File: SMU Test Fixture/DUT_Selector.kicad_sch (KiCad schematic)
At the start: 19 parts

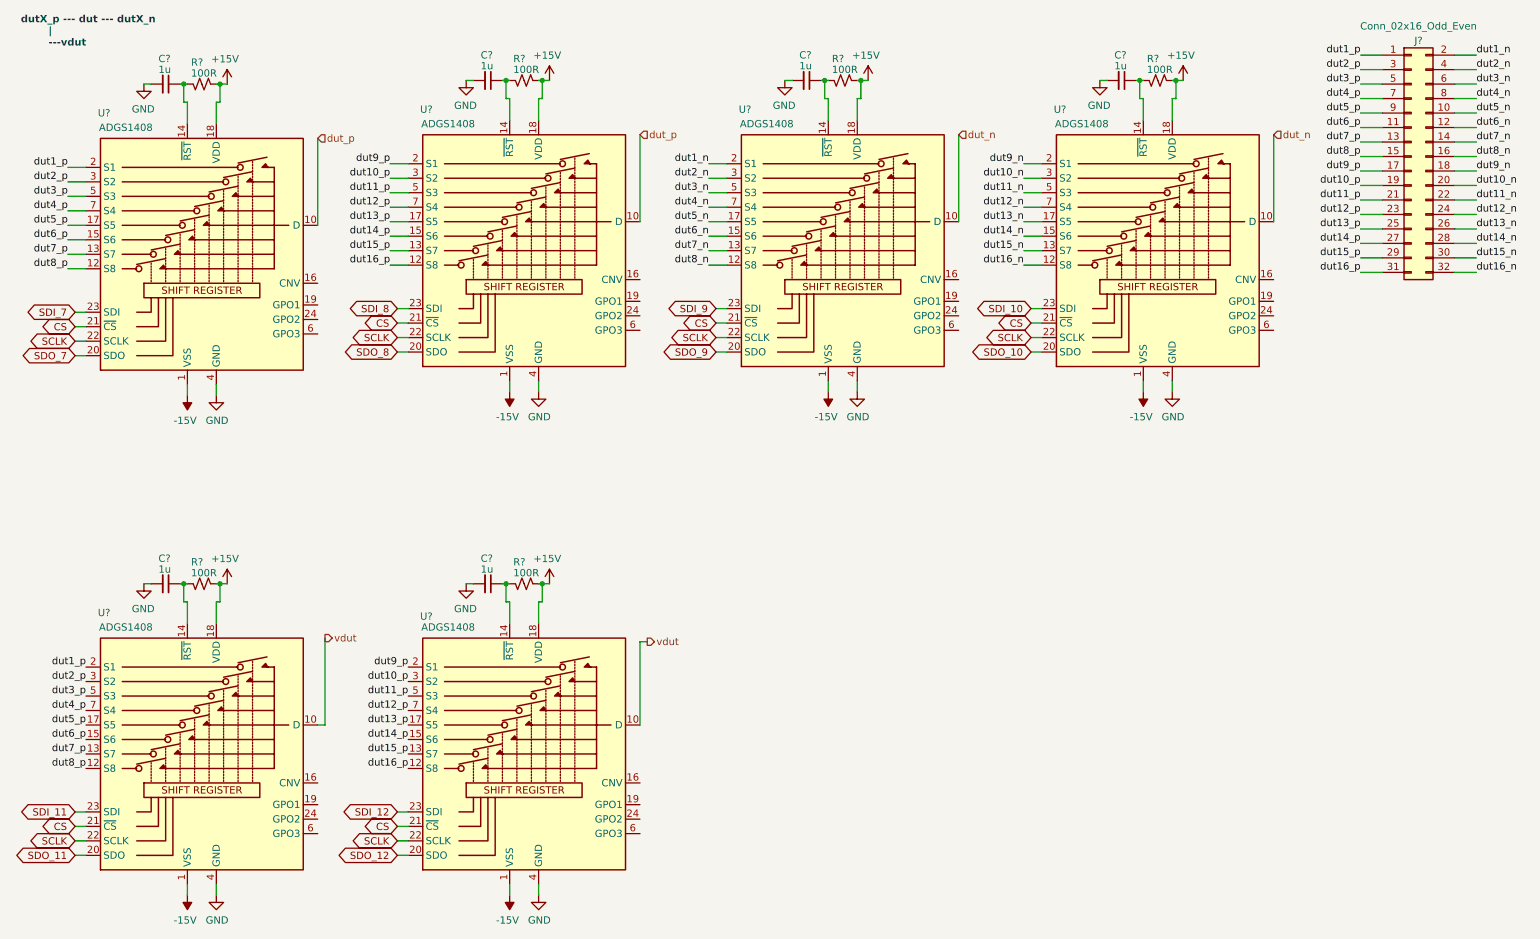
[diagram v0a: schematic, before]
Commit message: Fix grid nightmare. Begin adding bypass caps for a.switches
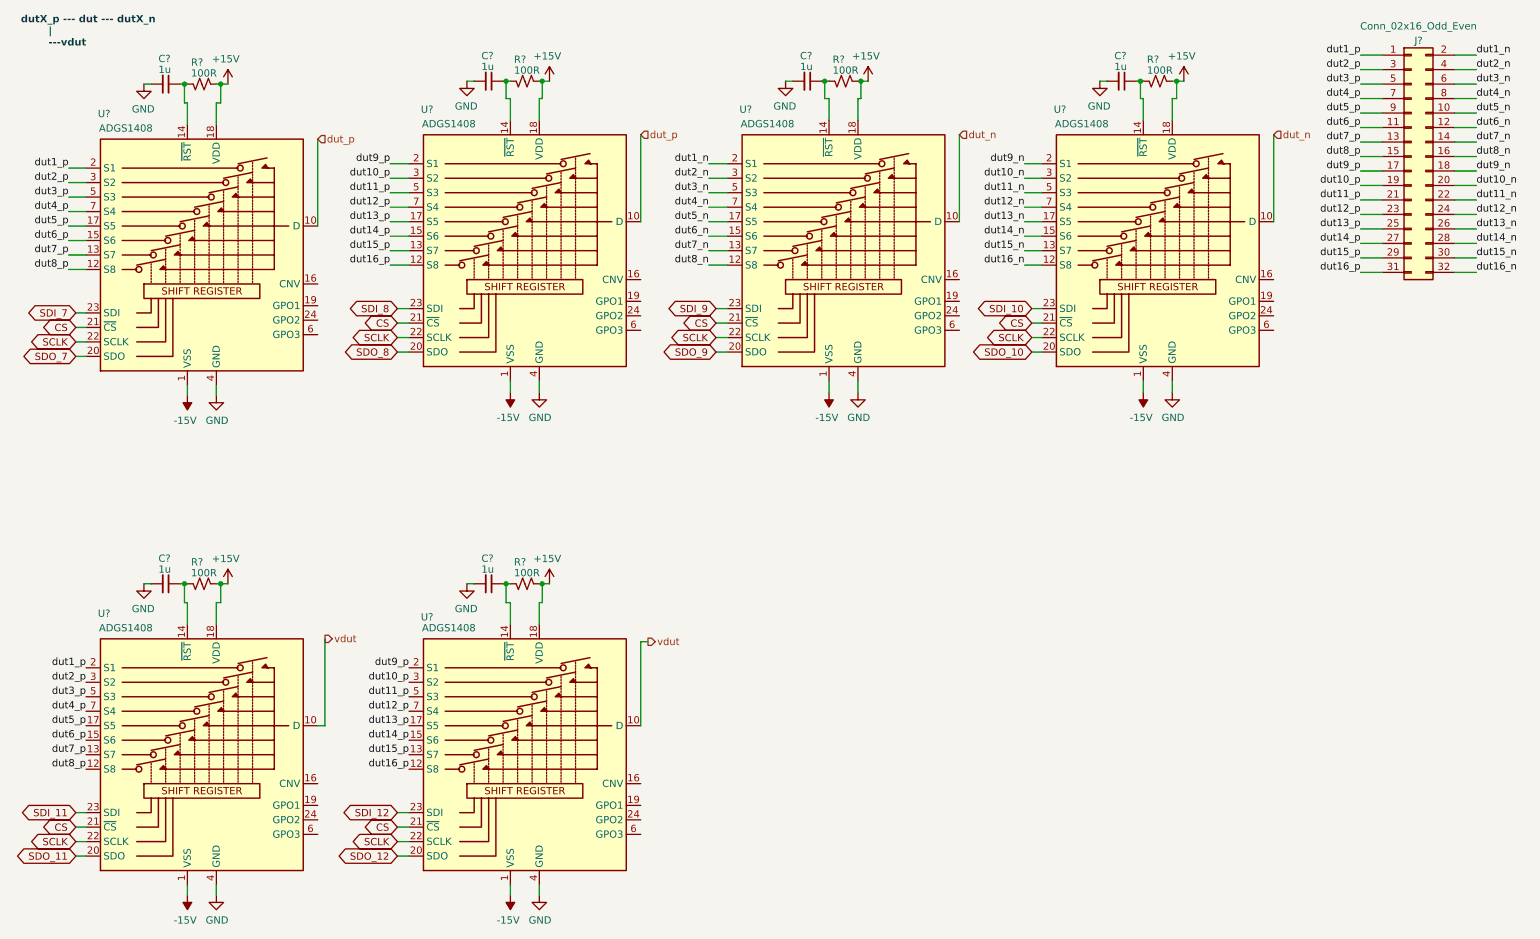
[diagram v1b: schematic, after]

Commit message: Finish adding bypass for all a.switches
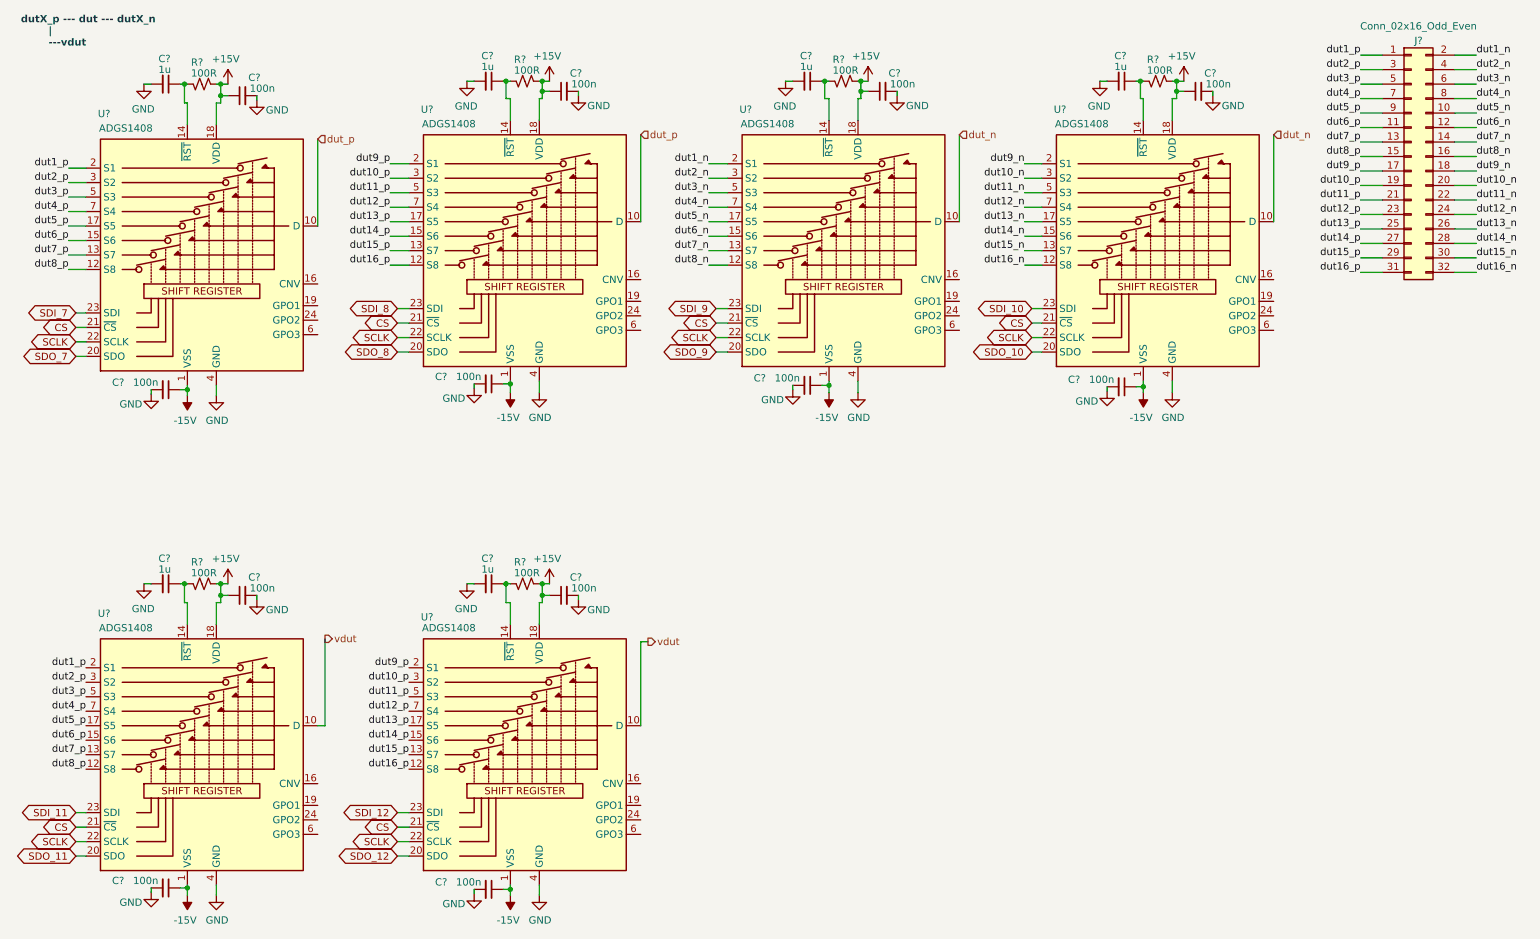
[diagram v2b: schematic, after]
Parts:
- added C? (x12): 100n, Capacitor_SMD:C_0805_2012Metric_Pad1.18x1.45mm_HandSolder, symbol Device:C_Small
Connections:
- net +15V: now also C?.1, C?.1, C?.1, C?.1, C?.1, C?.1
- net -15V: now also C?.1, C?.1, C?.1, C?.1, C?.1, C?.1
- net GND: now also C?.2, C?.2, C?.2, C?.2, C?.2, C?.2, C?.2, C?.2, C?.2, C?.2, C?.2, C?.2

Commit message: Split ADGS1408 units, add switch contorl page
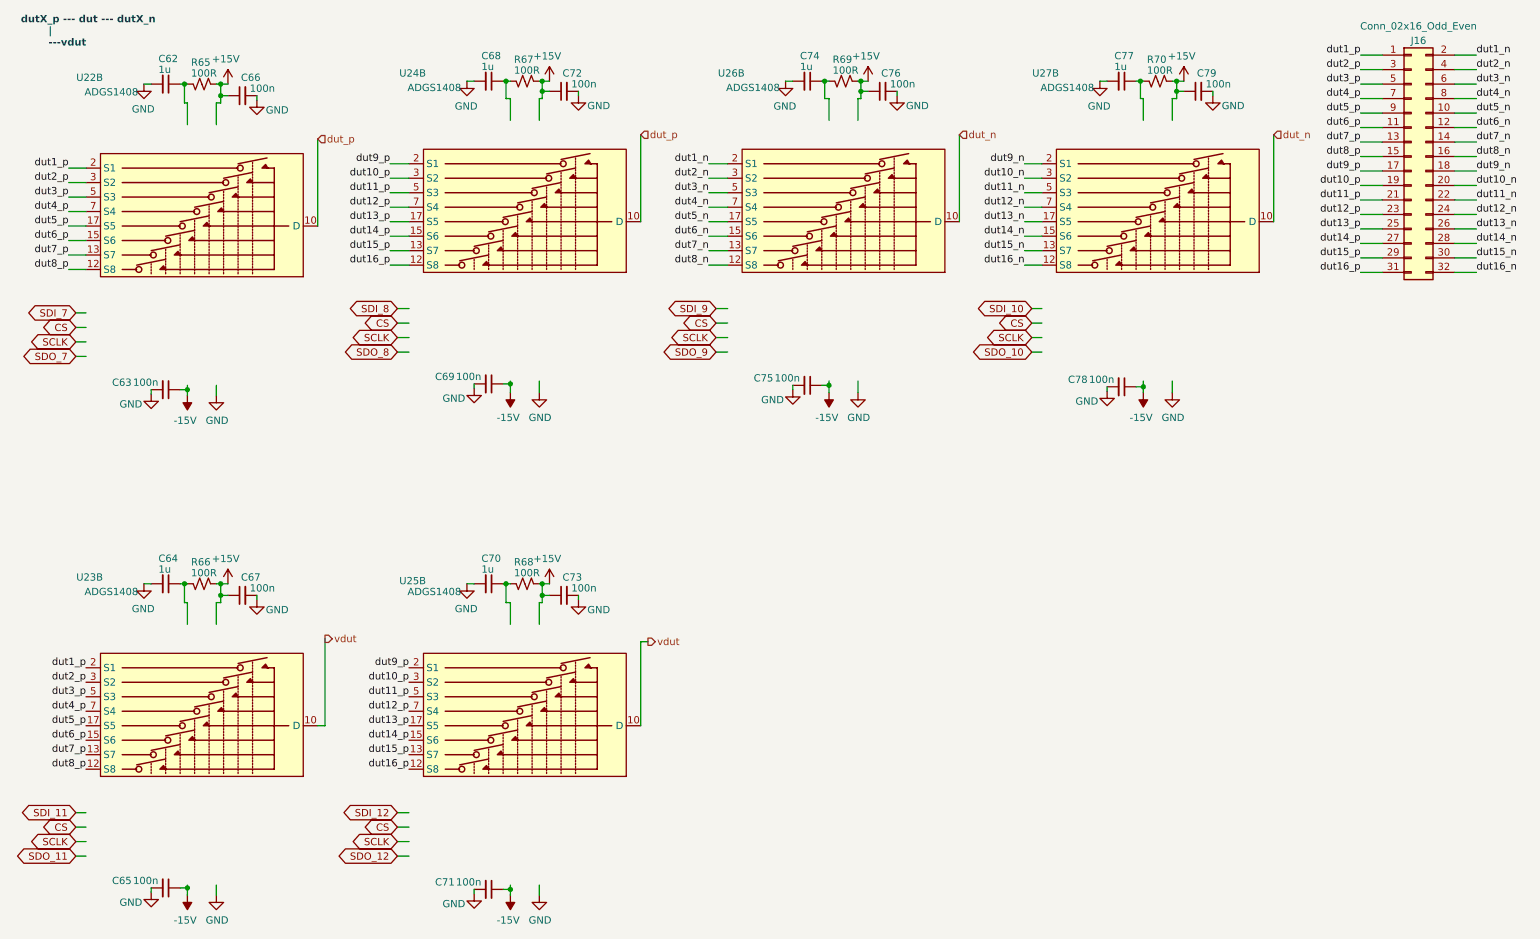
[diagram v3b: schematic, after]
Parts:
- gave numbers to parts that had none: 31
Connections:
- net +15V: no longer U22.18 (VDD), U23.18 (VDD), U24.18 (VDD), U25.18 (VDD), U26.18 (VDD), U27.18 (VDD)
- net -15V: no longer U22.1 (VSS), U22.25 (VSS), U23.1 (VSS), U23.25 (VSS), U24.1 (VSS), U24.25 (VSS), U25.1 (VSS), U25.25 (VSS), U26.1 (VSS), U26.25 (VSS), U27.1 (VSS), U27.25 (VSS)
- net CS: no longer U22.21 (~{CS}), U23.21 (~{CS}), U24.21 (~{CS}), U25.21 (~{CS}), U26.21 (~{CS}), U27.21 (~{CS})
- net GND: no longer U22.4 (GND), U23.4 (GND), U24.4 (GND), U25.4 (GND), U26.4 (GND), U27.4 (GND)
- net SCLK: no longer U22.22 (SCLK), U23.22 (SCLK), U24.22 (SCLK), U25.22 (SCLK), U26.22 (SCLK), U27.22 (SCLK)
- net SDI_10: no longer U27.23 (SDI)
- net SDI_11: no longer U23.23 (SDI)
- net SDI_12: no longer U25.23 (SDI)
- net SDI_7: no longer U22.23 (SDI)
- net SDI_8: no longer U24.23 (SDI)
- net SDI_9: no longer U26.23 (SDI)
- net SDO_10: no longer U27.20 (SDO)
- net SDO_11: no longer U23.20 (SDO)
- net SDO_12: no longer U25.20 (SDO)
- net SDO_7: no longer U22.20 (SDO)
- net SDO_8: no longer U24.20 (SDO)
- net SDO_9: no longer U26.20 (SDO)
- net at C62.1, R65.2: no longer U22.14 (~{RST})
- net at C68.1, R67.2: no longer U24.14 (~{RST})
- net at C74.1, R69.2: no longer U26.14 (~{RST})
- net at C77.1, R70.2: no longer U27.14 (~{RST})
- net at C64.1, R66.2: no longer U23.14 (~{RST})
- net at C70.1, R68.2: no longer U25.14 (~{RST})

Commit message: Symbol fixes, ERC pass
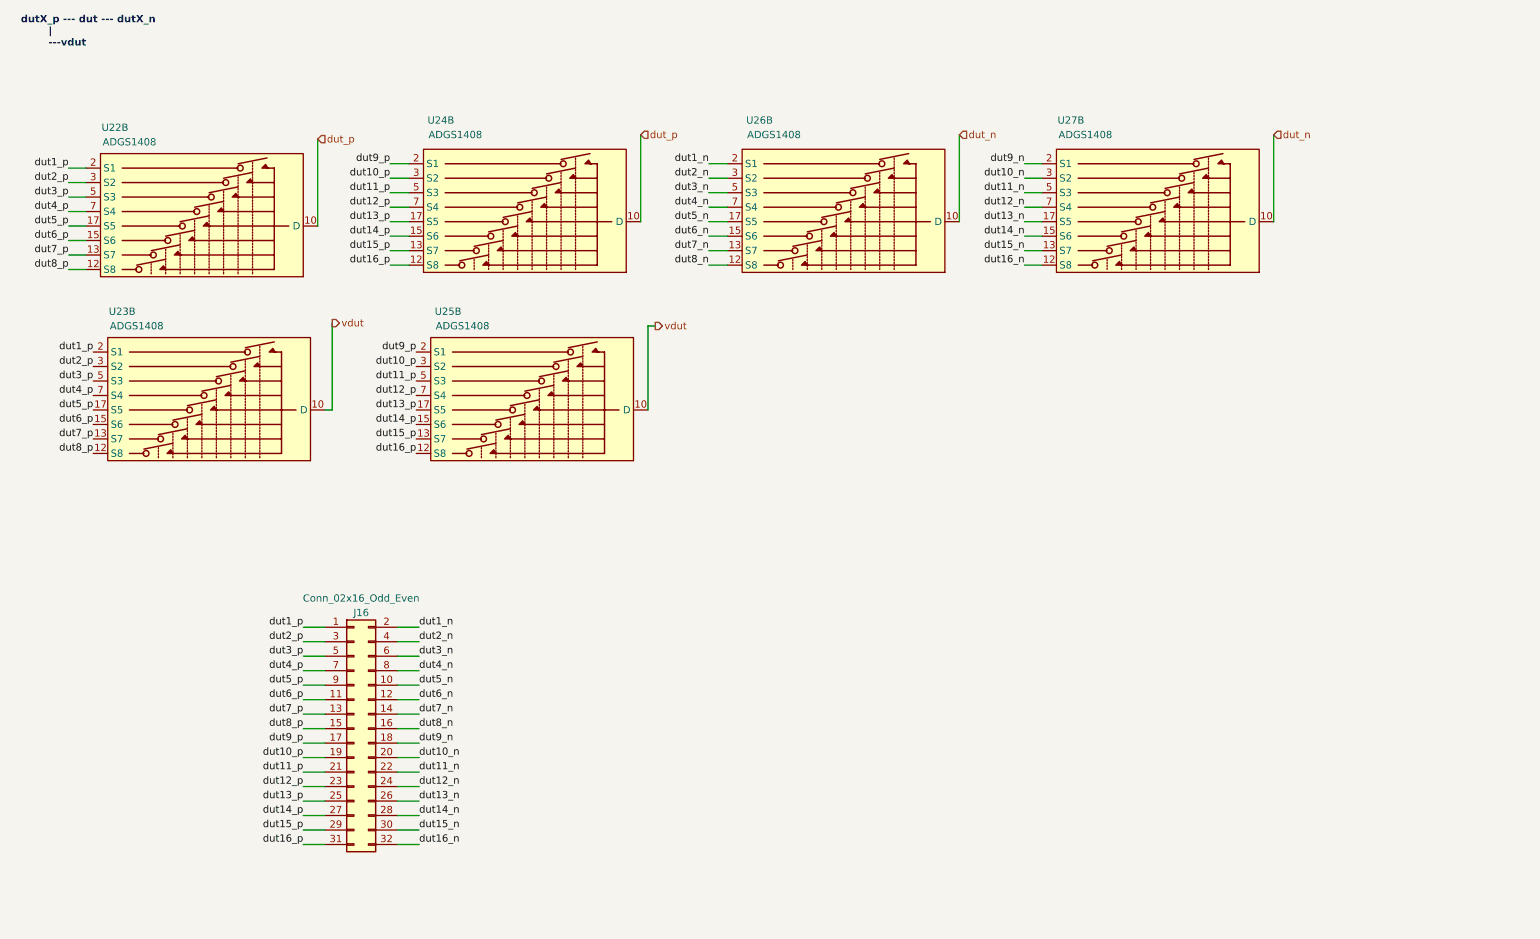
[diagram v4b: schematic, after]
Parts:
- removed C62, C64, C68, C70, C74, C77: 1u, symbol Device:C_Small
- removed C63, C65, C66, C67, C69, C71, C72, C73, C75, C76, C78, C79: 100n, Capacitor_SMD:C_0805_2012Metric_Pad1.18x1.45mm_HandSolder, symbol Device:C_Small
- removed R65, R66, R67, R68, R69, R70: 100R, symbol Device:R_Small_US
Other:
- moved on the sheet: J16, U23B, U25B
